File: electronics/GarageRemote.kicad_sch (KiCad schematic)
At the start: 33 parts, among them J1 CC1101 Module, J2 SERIAL, J3 ICSP, U1 TXS0108EPW, U2 ATmega328P-A, U3 MAX7060ATGT, Y1 16MHz, Y2 14.318MHz

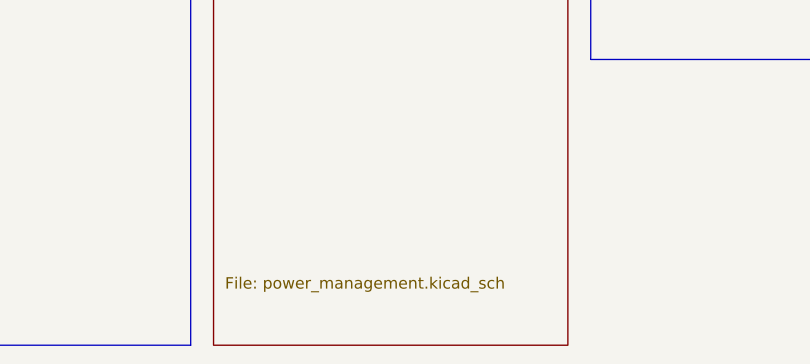
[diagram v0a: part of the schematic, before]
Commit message: Improve readme & rename files
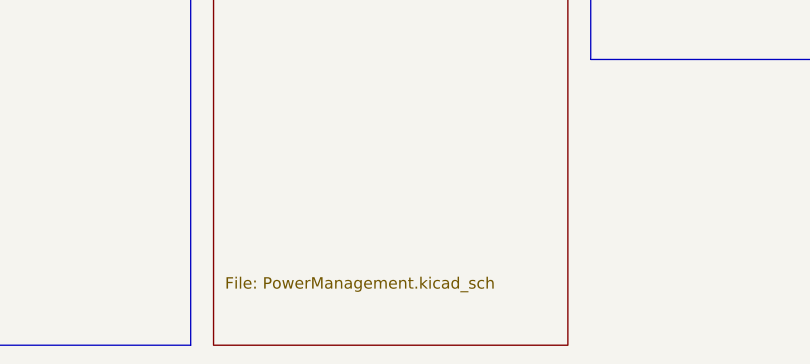
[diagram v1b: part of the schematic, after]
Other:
- sheet Power Management: file power_management.kicad_sch -> PowerManagement.kicad_sch

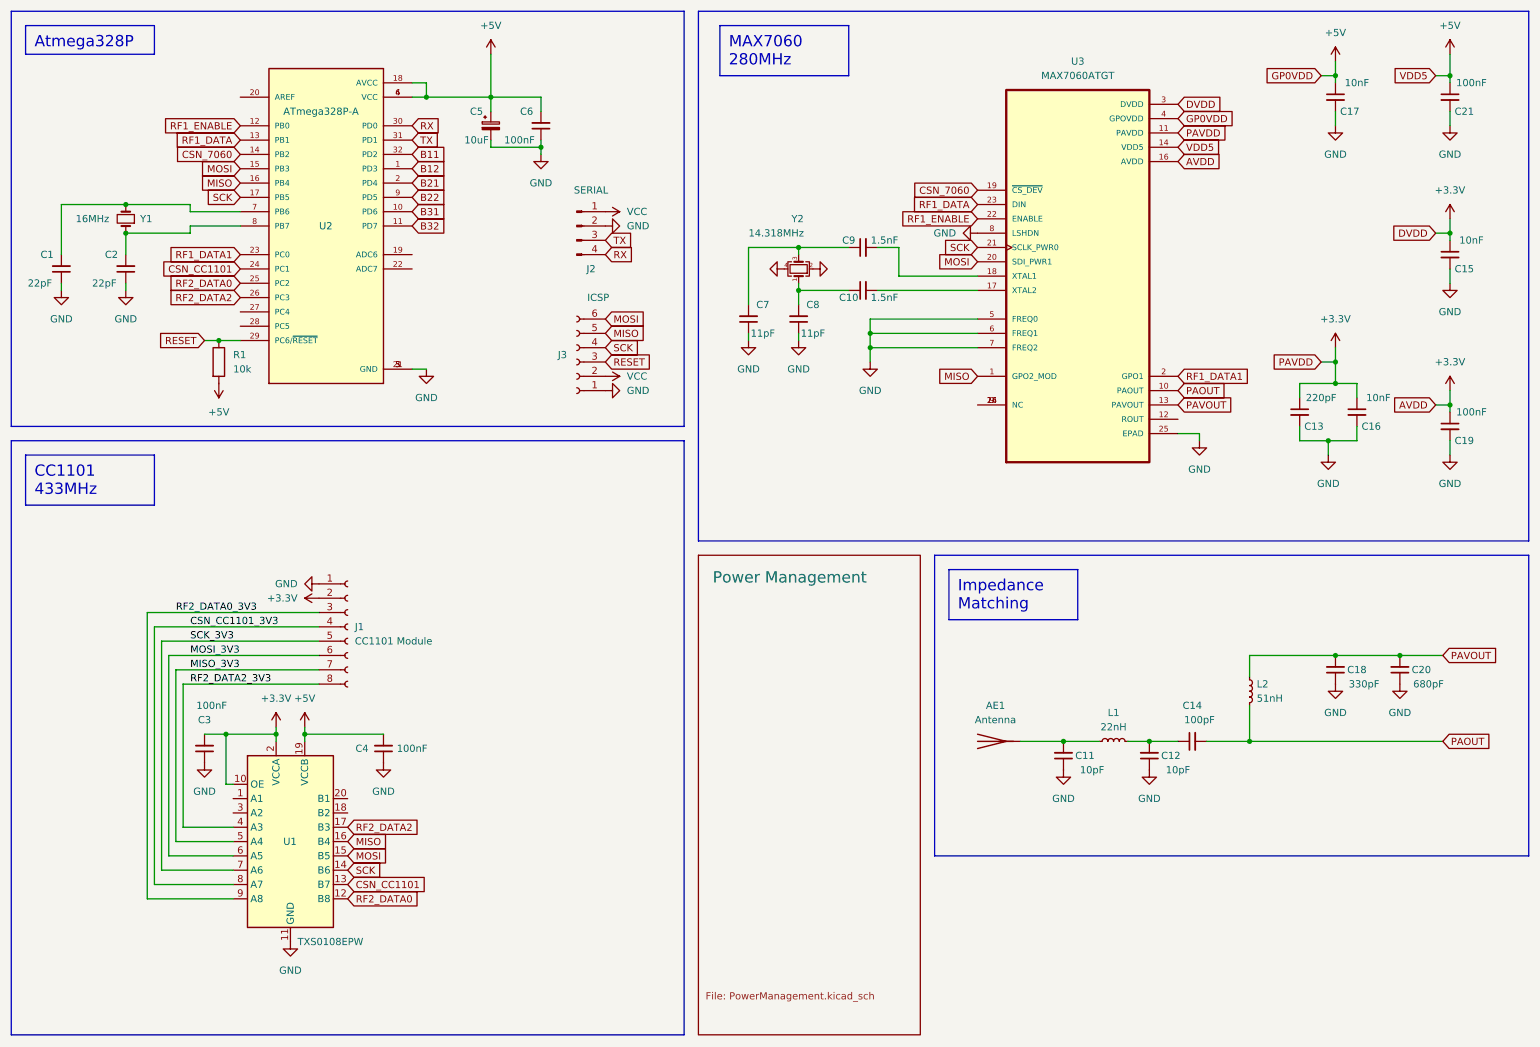
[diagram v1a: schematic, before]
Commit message: Implement second PCB iteration
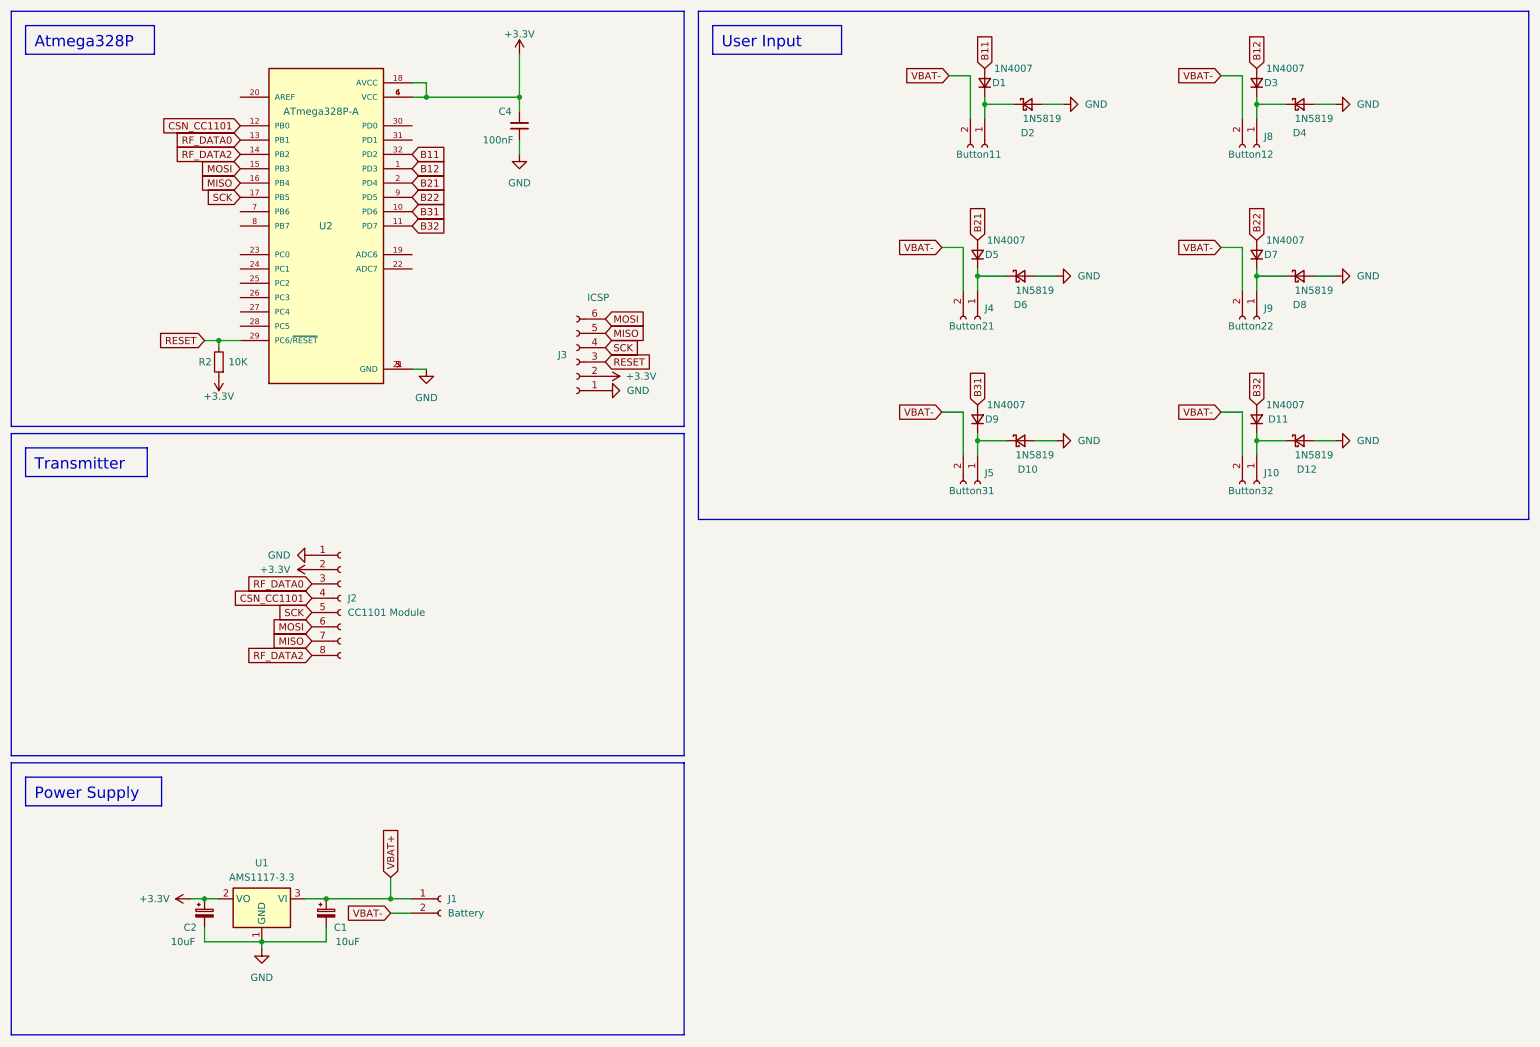
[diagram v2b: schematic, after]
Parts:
- removed AE1: Antenna, AA_Footprints:SMA-J-P-X-ST-EM1_EdgeMount, symbol Device:Antenna
- removed C1, C2: 22pF, Capacitor_SMD:C_0805_2012Metric_Pad1.18x1.45mm_HandSolder, symbol Device:C_Small
- removed C10, C9: 1.5nF, Capacitor_SMD:C_0805_2012Metric_Pad1.18x1.45mm_HandSolder, symbol Device:C_Small
- removed C11, C12: 10pF, Capacitor_SMD:C_0805_2012Metric_Pad1.18x1.45mm_HandSolder, symbol Device:C_Small
- removed C13: 220pF, Capacitor_SMD:C_0805_2012Metric_Pad1.18x1.45mm_HandSolder, symbol Device:C_Small
- removed C14: 100pF, Capacitor_SMD:C_0805_2012Metric_Pad1.18x1.45mm_HandSolder, symbol Device:C_Small
- removed C15, C16, C17: 10nF, Capacitor_SMD:C_0805_2012Metric_Pad1.18x1.45mm_HandSolder, symbol Device:C_Small
- removed C18: 330pF, Capacitor_SMD:C_0805_2012Metric_Pad1.18x1.45mm_HandSolder, symbol Device:C_Small
- removed C19, C21, C3, C4: 100nF, Capacitor_SMD:C_1210_3225Metric_Pad1.33x2.70mm_HandSolder, symbol Device:C_Small
- removed C20: 680pF, Capacitor_SMD:C_0805_2012Metric_Pad1.18x1.45mm_HandSolder, symbol Device:C_Small
- removed C5: 10uF, Capacitor_SMD:CP_Elec_6.3x4.9, symbol Device:C_Polarized_Small
- removed C7, C8: 11pF, Capacitor_SMD:C_0805_2012Metric_Pad1.18x1.45mm_HandSolder, symbol Device:C_Small
- removed J1: CC1101 Module, AA_Footprints:PE07-M1101D-SMA, symbol Connector:Conn_01x08_Socket
- removed J2: SERIAL, Connector_PinHeader_2.54mm:PinHeader_1x04_P2.54mm_Vertical, symbol Connector:Conn_01x04_Pin
- removed L1: 22nH, Inductor_SMD:L_0805_2012Metric_Pad1.15x1.40mm_HandSolder, symbol Device:L_Small
- removed L2: 51nH, Inductor_SMD:L_0805_2012Metric_Pad1.15x1.40mm_HandSolder, symbol Device:L_Small
- removed R1: 10k, Resistor_SMD:R_1206_3216Metric_Pad1.30x1.75mm_HandSolder, symbol Device:R
- removed U1: TXS0108EPW, Package_SO:TSSOP-20_4.4x6.5mm_P0.65mm, symbol Logic_LevelTranslator:TXS0108EPW
- removed U3: MAX7060ATGT, AA_Footprints:MAX7060-TQFN24, symbol MAX7060ATGT:MAX7060ATGT
- removed Y1: 16MHz, Crystal:Crystal_HC49-4H_Vertical, symbol Device:Crystal_Small
- removed Y2: 14.318MHz, Crystal:Crystal_SMD_Abracon_ABM8G-4Pin_3.2x2.5mm, symbol Device:Crystal_GND24_Small
- added C1, C2: 10uF, Capacitor_SMD:CP_Elec_5x5.9, symbol Device:C_Polarized_Small
- added D1, D11, D3, D5, D7, D9: 1N4007, Diode_SMD:D_SOD-523, symbol Device:D_Small
- added D10, D12, D2, D4, D6, D8: 1N5819, Diode_SMD:D_SOD-523, symbol Device:D_Schottky_Small
- added J1: Battery, AA_Footprints:BS-2032-3, symbol Connector:Conn_01x02_Socket
- added J10: Button32, AA_Footprints:4.5mm switch, symbol Connector:Conn_01x02_Socket
- added J2: CC1101 Module, AA_Footprints:PE07-M1101D-SMA, symbol Connector:Conn_01x08_Socket
- added J4: Button21, AA_Footprints:4.5mm switch, symbol Connector:Conn_01x02_Socket
- added J5: Button31, AA_Footprints:4.5mm switch, symbol Connector:Conn_01x02_Socket
- added J7: Button11, AA_Footprints:4.5mm switch, symbol Connector:Conn_01x02_Socket
- added J8: Button12, AA_Footprints:4.5mm switch, symbol Connector:Conn_01x02_Socket
- added J9: Button22, AA_Footprints:4.5mm switch, symbol Connector:Conn_01x02_Socket
- added R2: 10K, Resistor_SMD:R_1206_3216Metric_Pad1.30x1.75mm_HandSolder, symbol Device:R_Small
- added U1: AMS1117-3.3, Package_TO_SOT_SMD:SOT-223-3_TabPin2, symbol Regulator_Linear:AMS1117-3.3
- renumbered C6 to C4
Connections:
- net +5V is gone; now on net +3.3V: C4.2, U2.18 (AVCC), U2.4 (VCC), U2.6 (VCC)
- net RF1_ENABLE is gone; now on net CSN_CC1101: U2.12 (PB0)
- net VCC is gone; now on net +3.3V: J3.2 (Pin_2)
- net +3.3V: now also C2.1, J2.2 (Pin_2), R2.1, U1.2 (VO)
- net B11: now also D1.2 (A)
- net B12: now also D3.2 (A)
- net B21: now also D5.2 (A)
- net B22: now also D7.2 (A)
- net B31: now also D9.2 (A)
- net B32: now also D11.2 (A)
- net CSN_CC1101: now also J2.4 (Pin_4); no longer U2.24 (PC1)
- net GND: now also C1.2, C2.2, D10.2 (A), D12.2 (A), D2.2 (A), D4.2 (A), D6.2 (A), D8.2 (A), J2.1 (Pin_1), U1.1 (GND)
- net MISO: now also J2.7 (Pin_7)
- net MOSI: now also J2.6 (Pin_6)
- net RESET: now also R2.2
- net SCK: now also J2.5 (Pin_5)
- net CSN_7060 renamed RF_DATA2
- net RF_DATA2: now also J2.8 (Pin_8)
- net RF1_DATA renamed RF_DATA0
- net RF_DATA0: now also J2.3 (Pin_3)
- net RF1_DATA1: no longer names the net of U2.23 (PC0)
- net RF2_DATA0: no longer names the net of U2.25 (PC2)
- net RF2_DATA2: no longer names the net of U2.26 (PC3)
- net RX: no longer names the net of U2.30 (PD0)
- net TX: no longer names the net of U2.31 (PD1)
- new net: D1.1 (K), D2.1 (K), J7.1 (Pin_1)
- new net: D3.1 (K), D4.1 (K), J8.1 (Pin_1)
- new net: D7.1 (K), D8.1 (K), J9.1 (Pin_1)
- new net: D10.1 (K), D9.1 (K), J5.1 (Pin_1)
- new net: D5.1 (K), D6.1 (K), J4.1 (Pin_1)
- new net: D11.1 (K), D12.1 (K), J10.1 (Pin_1)
- new net VBAT+: C1.1, J1.1 (Pin_1), U1.3 (VI)
- new net VBAT-: J1.2 (Pin_2), J10.2 (Pin_2), J4.2 (Pin_2), J5.2 (Pin_2), J7.2 (Pin_2), J8.2 (Pin_2), J9.2 (Pin_2)
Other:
- removed sheet Power Management
- title: Garage Remote -> Garage Remote Lite
- moved on the sheet: C4

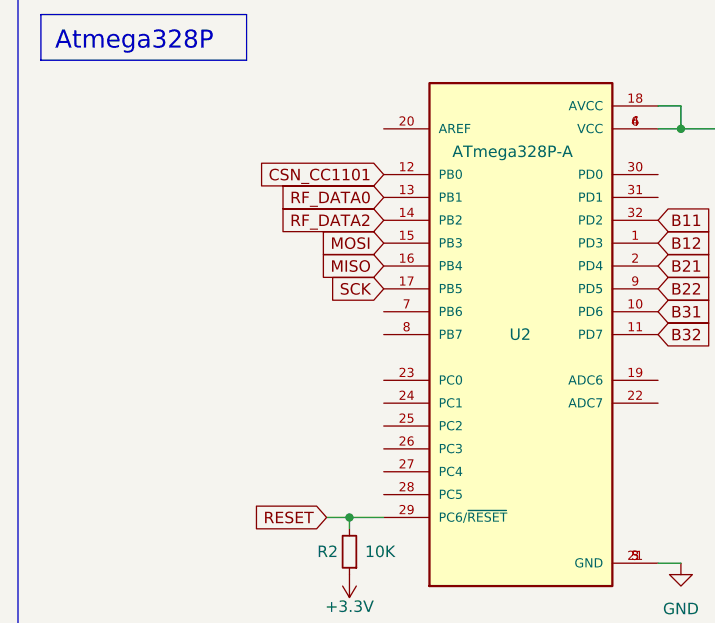
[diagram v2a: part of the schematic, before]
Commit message: Fix ground plane
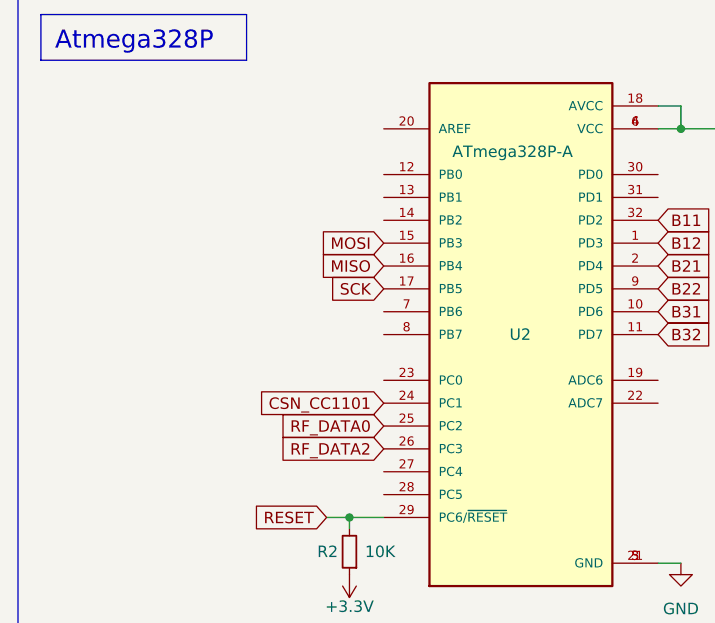
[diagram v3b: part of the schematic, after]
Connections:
- net CSN_CC1101: now also U2.24 (PC1); no longer U2.12 (PB0)
- net RF_DATA0: now also U2.25 (PC2); no longer U2.13 (PB1)
- net RF_DATA2: now also U2.26 (PC3); no longer U2.14 (PB2)
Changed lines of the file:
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@@
+    )
+  )
+  (global_label "RF_DATA0" (shape input) (at 54.61 62.23 180) (fields_autoplaced)
+    (effects (font (size 1.27 1.27)) (justify right))
+    (property "Intersheetrefs" "${INTERSHEET_REFS}" (at 42.6743 62.23 0)
+      (effects (font (size 1.27 1.27)) (justify right) hide)
     )
   )
@@
     )
   )
-  (global_label "RF_DATA0" (shape input) (at 54.61 36.83 180) (fields_autoplaced)
-    (effects (font (size 1.27 1.27)) (justify right))
-    (property "Intersheetrefs" "${INTERSHEET_REFS}" (at 42.6743 36.83 0)
-      (effects (font (size 1.27 1.27)) (justify right) hide)
-    )
-  )
   (global_label "VBAT-" (shape input) (at 228.6 25.4 180) (fields_autoplaced)
     (effects (font (size 1.27 1.27)) (justify right))
@@
     )
   )
-  (global_label "CSN_CC1101" (shape input) (at 54.61 34.29 180) (fields_autoplaced)
+  (global_label "RF_DATA2" (shape input) (at 54.61 64.77 180) (fields_autoplaced)
     (effects (font (size 1.27 1.27)) (justify right))
-    (property "Intersheetrefs" "${INTERSHEET_REFS}" (at 39.4692 34.29 0)
+    (property "Intersheetrefs" "${INTERSHEET_REFS}" (at 42.6743 64.77 0)
       (effects (font (size 1.27 1.27)) (justify right) hide)
     )
@@
     )
   )
-  (global_label "RF_DATA2" (shape input) (at 54.61 39.37 180) (fields_autoplaced)
+  (global_label "CSN_CC1101" (shape input) (at 54.61 59.69 180) (fields_autoplaced)
     (effects (font (size 1.27 1.27)) (justify right))
-    (property "Intersheetrefs" "${INTERSHEET_REFS}" (at 42.6743 39.37 0)
+    (property "Intersheetrefs" "${INTERSHEET_REFS}" (at 39.4692 59.69 0)
       (effects (font (size 1.27 1.27)) (justify right) hide)
     )
